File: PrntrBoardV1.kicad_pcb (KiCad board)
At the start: 4 copper layers, 99 x 99 mm, 238 parts, among them J1 EXT 5V, J10 Probe, J11 Extruder Heater, J12 Stepper, J13 Thermistor, J14 Max, J15 Min, J16 Max, J17 Min, J18 Max, J19 Min, J2 Bed Heater, J20 Stepper, J21 Stepper, J22 Stepper, J23 Stepper, J24 Probe, J25 Extruder Heater, J26 Stepper, J27 Thermistor, J28 Thermistor, J29 12-24V, J3 Z Probe, J30 LCD, J31 TC1, J32 TC2, J33 Vin, J34 Vin, J35 5V, J36 5V, J4 E0 Cool, J5 E0 Part, J6 E1 Cool, J7 E1 Part, J8 Always On Fan 1, J9 Always On Fan 2, U1 4078, U11 NUCLEO-64, U2 74HCT02, U3 74LVC125, U4 TMC5130, U5 TMC5130, U6 TMC5130, U7 TMC5130, U8 TMC5130, X1 16MHz

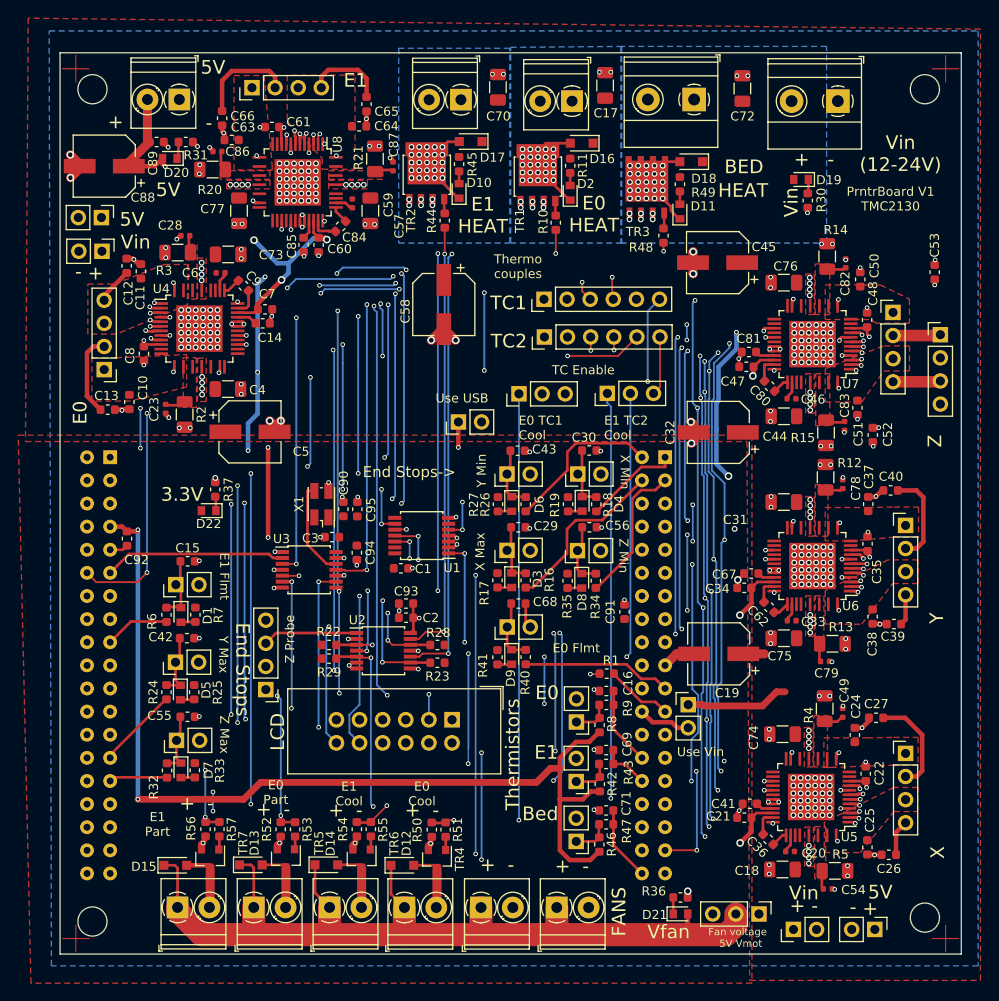
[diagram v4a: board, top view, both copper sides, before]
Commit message: Add thermal releaf on most truehole connectors.
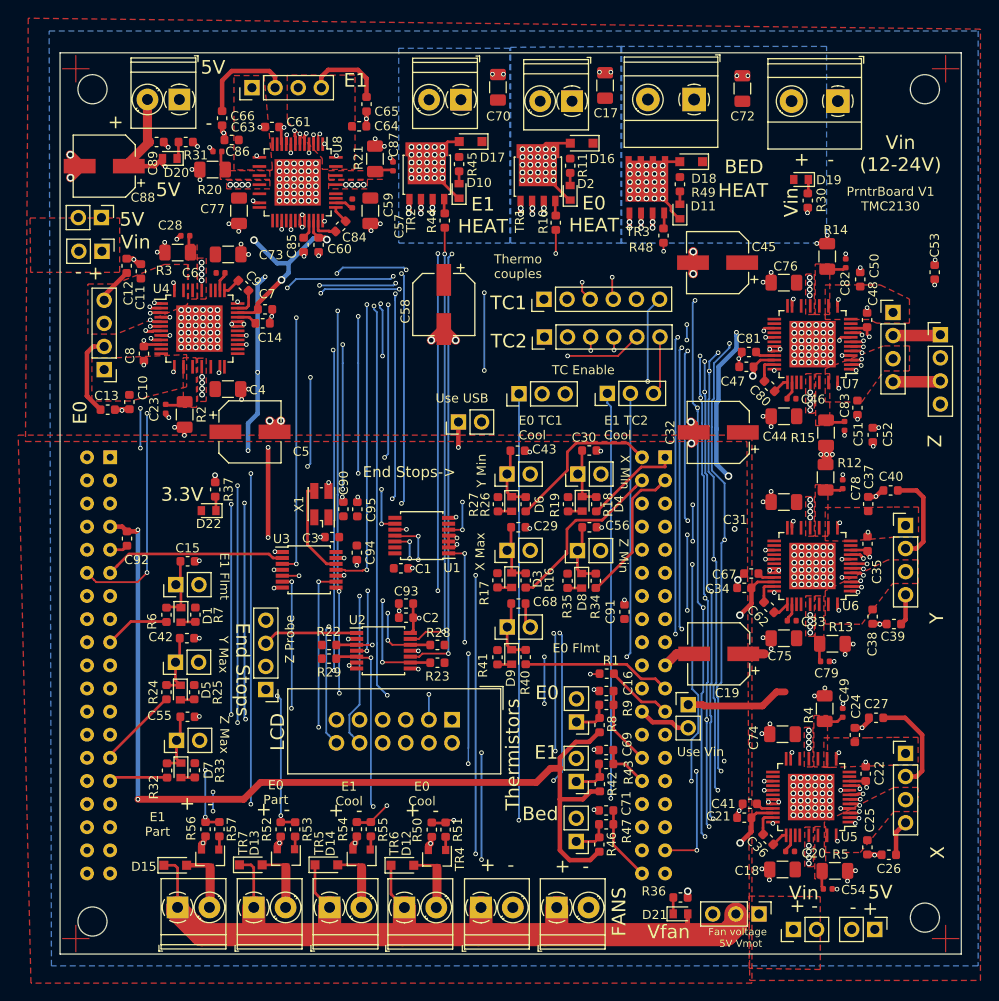
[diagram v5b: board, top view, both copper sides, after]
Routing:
- net GND: track 110.9 -> 170.3 mm, vias 366 -> 365
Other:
- board text added: "(c) iQury.us Aug 2018"
- board text added: "Btn In"
- board text added: "Enc A"
- board text added: "Enc B"
- board text removed: "(c) iQury.us July 2018"

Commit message: Rellocate internal fan connectors, so they are out of the way of the nucleo board. Removed all footprint references from the silk screen.
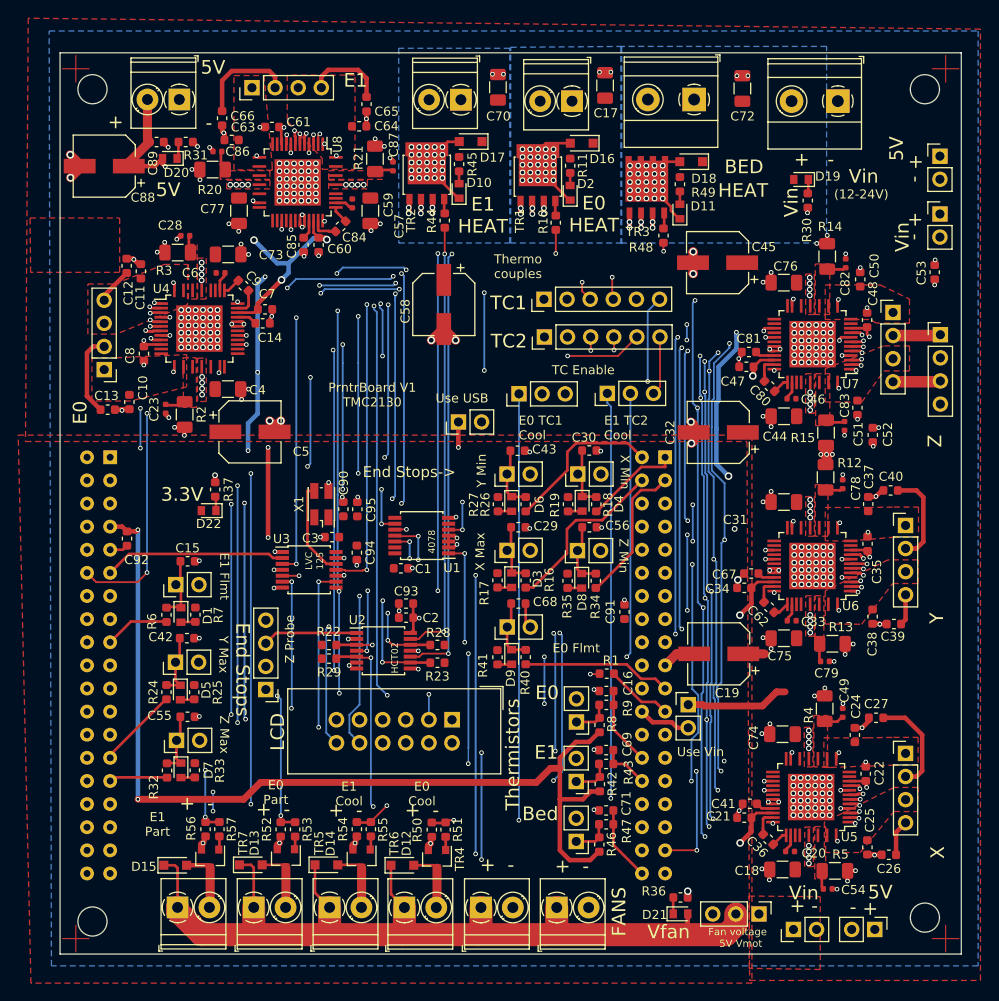
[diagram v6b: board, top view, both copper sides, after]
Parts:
- moved J35 92.4 mm to (116.6, 30.4), turned to 0 degrees
- moved J33 92.1 mm to (116.6, 36.7), turned to 0 degrees
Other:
- board text added: "(12-24V)"
- board text added: "4078"
- board text added: "HCT02"
- board text added: "LVC 125"
- board text removed: "Vin (12-24V)"
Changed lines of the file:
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@@
-(kicad_pcb (version 20171130) (host pcbnew 6.0.0-rc1-unknown-13b9679~65~ubuntu18.04.1)
+(kicad_pcb (version 20171130) (host pcbnew 6.0.0-rc1-unknown-fd3e57d~66~ubuntu18.04.1)
   (general
     (thickness 1.6)
-    (drawings 137)
+    (drawings 142)
     (tracks 2723)
     (zones 0)
@@
   )
   (setup
-    (last_trace_width 0.2032)
+    (last_trace_width 0.1524)
     (user_trace_width 0.1524)
     (user_trace_width 0.2032)
@@
       (psnegative false)
       (psa4output false)
-      (plotreference true)
+      (plotreference false)
       (plotvalue false)
       (plotinvisibletext false)
@@
   )
   (module Connector_PinHeader_2.54mm:PinHeader_1x02_P2.54mm_Vertical (layer F.Cu)
-    (at 24.6 40.8 270)
+    (at 116.6495 36.703)
     (descr "Through hole straight pin header, 1x02, 2.54mm pitch, single row")
     (tags "Through hole pin header THT 1x02 2.54mm single row")
-    (fp_text reference J33 (at -0.1 -0.51 270) (layer F.SilkS) hide
+    (fp_text reference J33 (at -0.1 -0.51) (layer F.SilkS) hide
       (effects (font (size 1 1) (thickness 0.15)))
     )
-    (fp_text value Vin (at 0 4.87 270) (layer F.Fab)
+    (fp_text value Vin (at 0 4.87) (layer F.Fab)
       (effects (font (size 1 1) (thickness 0.15)))
     )
-    (fp_text user %R (at 0 1.27) (layer F.Fab)
+    (fp_text user %R (at 0 1.27 -270) (layer F.Fab)
       (effects (font (size 1 1) (thickness 0.15)))
     )
@@
     (fp_line (start 1.27 -1.27) (end 1.27 3.81) (layer F.Fab) (width 0.1))
     (fp_line (start -0.635 -1.27) (end 1.27 -1.27) (layer F.Fab) (width 0.1))
-    (pad 2 thru_hole oval (at 0 2.54 270) (size 1.7 1.7) (drill 1) (layers *.Cu *.Mask)
+    (pad 2 thru_hole oval (at 0 2.54) (size 1.7 1.7) (drill 1) (layers *.Cu *.Mask)
       (net 8 GND))
-    (pad 1 thru_hole rect (at 0 0 270) (size 1.7 1.7) (drill 1) (layers *.Cu *.Mask)
+    (pad 1 thru_hole rect (at 0 0) (size 1.7 1.7) (drill 1) (layers *.Cu *.Mask)
       (net 1 /V_MOTORS))
     (model ${KISYS3DMOD}/Connector_PinHeader_2.54mm.3dshapes/PinHeader_1x02_P2.54mm_Vertical.wrl
@@
   )
   (module Connector_PinHeader_2.54mm:PinHeader_1x02_P2.54mm_Vertical (layer F.Cu)
-    (at 24.54 37.1 270)
+    (at 116.6495 30.353)
     (descr "Through hole straight pin header, 1x02, 2.54mm pitch, single row")
     (tags "Through hole pin header THT 1x02 2.54mm single row")
-    (fp_text reference J35 (at -0.05 -0.75 270) (layer F.SilkS) hide
+    (fp_text reference J35 (at -0.05 -0.75) (layer F.SilkS) hide
       (effects (font (size 1 1) (thickness 0.15)))
     )
-    (fp_text value 5V (at 0 4.87 270) (layer F.Fab)
+    (fp_text value 5V (at 0 4.87) (layer F.Fab)
       (effects (font (size 1 1) (thickness 0.15)))
     )
-    (fp_text user %R (at 0 1.27) (layer F.Fab)
+    (fp_text user %R (at 0 1.27 -270) (layer F.Fab)
       (effects (font (size 1 1) (thickness 0.15)))
     )
@@
     (fp_line (start 1.27 -1.27) (end 1.27 3.81) (layer F.Fab) (width 0.1))
     (fp_line (start -0.635 -1.27) (end 1.27 -1.27) (layer F.Fab) (width 0.1))
-    (pad 2 thru_hole oval (at 0 2.54 270) (size 1.7 1.7) (drill 1) (layers *.Cu *.Mask)
+    (pad 2 thru_hole oval (at 0 2.54) (size 1.7 1.7) (drill 1) (layers *.Cu *.Mask)
       (net 8 GND))
-    (pad 1 thru_hole rect (at 0 0 270) (size 1.7 1.7) (drill 1) (layers *.Cu *.Mask)
+    (pad 1 thru_hole rect (at 0 0) (size 1.7 1.7) (drill 1) (layers *.Cu *.Mask)
       (net 10 /5V))
     (model ${KISYS3DMOD}/Connector_PinHeader_2.54mm.3dshapes/PinHeader_1x02_P2.54mm_Vertical.wrl
@@
     (tags diode)
     (attr smd)
-    (fp_text reference D19 (at -3.0532 -0.0566 180) (layer F.SilkS)
+    (fp_text reference D19 (at -2.9337 0.3429 180) (layer F.SilkS)
       (effects (font (size 1 1) (thickness 0.15)))
     )
@@
     (tags resistor)
     (attr smd)
-    (fp_text reference R30 (at -0.0548 -1.4916 270) (layer F.SilkS)
+    (fp_text reference R30 (at 3.2512 0.0889 270) (layer F.SilkS)
       (effects (font (size 1 1) (thickness 0.15)))
     )
@@
     (tags capacitor)
     (attr smd)
-    (fp_text reference C53 (at -2.9592 0 270) (layer F.SilkS)
+    (fp_text reference C53 (at 0.08 1.4575 270) (layer F.SilkS)
       (effects (font (size 1 1) (thickness 0.15)))
     )
@@
     (tags resistor)
     (attr smd)
-    (fp_text reference R14 (at 2.919 0.933 -180) (layer F.SilkS)
+    (fp_text reference R14 (at 3.269 0.3175 -180) (layer F.SilkS)
       (effects (font (size 1 1) (thickness 0.15)))
     )
@@
     )
   )
+  (gr_text "LVC\n125" (at 47.9425 74.803 90) (layer F.SilkS)
+    (effects (font (size 0.75 0.75) (thickness 0.15)))
+  )
+  (gr_text 4078 (at 60.833 72.7075 90) (layer F.SilkS)
+    (effects (font (size 0.75 0.75) (thickness 0.15)))
+  )
+  (gr_text HCT02 (at 56.769 85.471 90) (layer F.SilkS)
+    (effects (font (size 0.75 0.75) (thickness 0.15)))
+  )
+  (gr_text "+ -" (at 114.046 31.6865 270) (layer F.SilkS)
+    (effects (font (size 1.5 1.5) (thickness 0.3)))
+  )
+  (gr_text "(12-24V)" (at 108.0135 34.544) (layer F.SilkS)
+    (effects (font (size 1 1) (thickness 0.25)))
+  )
   (gr_text GND (at 50.3555 89.662 90) (layer B.SilkS)
     (effects (font (size 1 1) (thickness 0.15)) (justify mirror))
@@
   (gr_line (start 56 27) (end 56 55) (layer B.SilkS) (width 0.15))
   (gr_line (start 28 27) (end 56 27) (layer B.SilkS) (width 0.15))
-  (gr_text "+ -" (at 23.1 34.8) (layer B.SilkS)
+  (gr_text "+ -" (at 113.8555 31.6865 90) (layer B.SilkS)
     (effects (font (size 1.5 1.5) (thickness 0.3)) (justify mirror))
   )
-  (gr_text Vin (at 26.035 42.799) (layer B.SilkS)
+  (gr_text Vin (at 112.014 38.1635 90) (layer B.SilkS)
     (effects (font (size 1.5 1.5) (thickness 0.3)) (justify mirror))
   )
-  (gr_text "+ -" (at 23.1 38.9) (layer B.SilkS)
+  (gr_text "+ -" (at 113.792 38.0365 90) (layer B.SilkS)
     (effects (font (size 1.5 1.5) (thickness 0.3)) (justify mirror))
   )
-  (gr_text 5V (at 26.289 33.4645) (layer B.SilkS)
+  (gr_text 5V (at 112.141 31.8135 90) (layer B.SilkS)
     (effects (font (size 1.5 1.5) (thickness 0.3)) (justify mirror))
   )
@@
     (effects (font (size 1 1) (thickness 0.15)) (justify mirror))
   )
-  (gr_text Vin (at 28.3 39.8) (layer F.SilkS)
+  (gr_text Vin (at 112.522 39.243 90) (layer F.SilkS)
     (effects (font (size 1.5 1.5) (thickness 0.3)))
   )
-  (gr_text "+ -" (at 23.2 43.3 180) (layer F.SilkS)
+  (gr_text "+ -" (at 113.9825 38.0365 270) (layer F.SilkS)
     (effects (font (size 1.5 1.5) (thickness 0.3)))
   )
-  (gr_text 5V (at 27.9 37.3) (layer F.SilkS)
+  (gr_text 5V (at 111.887 29.5275 90) (layer F.SilkS)
     (effects (font (size 1.5 1.5) (thickness 0.3)))
   )
@@
     (effects (font (size 1 1) (thickness 0.2)))
   )
-  (gr_text "Vin\n(12-24V)" (at 112.3188 30.0736) (layer F.SilkS)
+  (gr_text Vin (at 108.2675 32.5755) (layer F.SilkS)
     (effects (font (size 1.5 1.5) (thickness 0.3)))
   )
@@
     (effects (font (size 1 1) (thickness 0.15)) (justify mirror))
   )
-  (gr_text "rev 3" (at 116.3 32.1 90) (layer B.SilkS)
+  (gr_text "rev 3" (at 103.3145 32.4485) (layer B.SilkS)
     (effects (font (size 1.5 1.5) (thickness 0.3)) (justify mirror))
   )
-  (gr_text "(c) iQury.us\nAug 2018" (at 113 32.5 90) (layer B.SilkS)
+  (gr_text "(c) iQury.us\nAug 2018" (at 103.124 35.4965) (layer B.SilkS)
     (effects (font (size 1 1) (thickness 0.15)) (justify mirror))
   )
-  (gr_text "PrntrBoard V1\nTMC2130" (at 111.2266 35.052) (layer F.SilkS)
+  (gr_text "PrntrBoard V1\nTMC2130" (at 54.2925 56.5785) (layer F.SilkS)
     (effects (font (size 1 1) (thickness 0.15)))
   )
@@
     (effects (font (size 1.5 1.5) (thickness 0.3)) (justify mirror))
   )
-  (gr_text "Z Axis" (at 114.2 43.9 90) (layer B.SilkS)
+  (gr_text "Z Axis" (at 114.7445 44.5135 90) (layer B.SilkS)
     (effects (font (size 1.5 1.5) (thickness 0.3)) (justify mirror))
   )

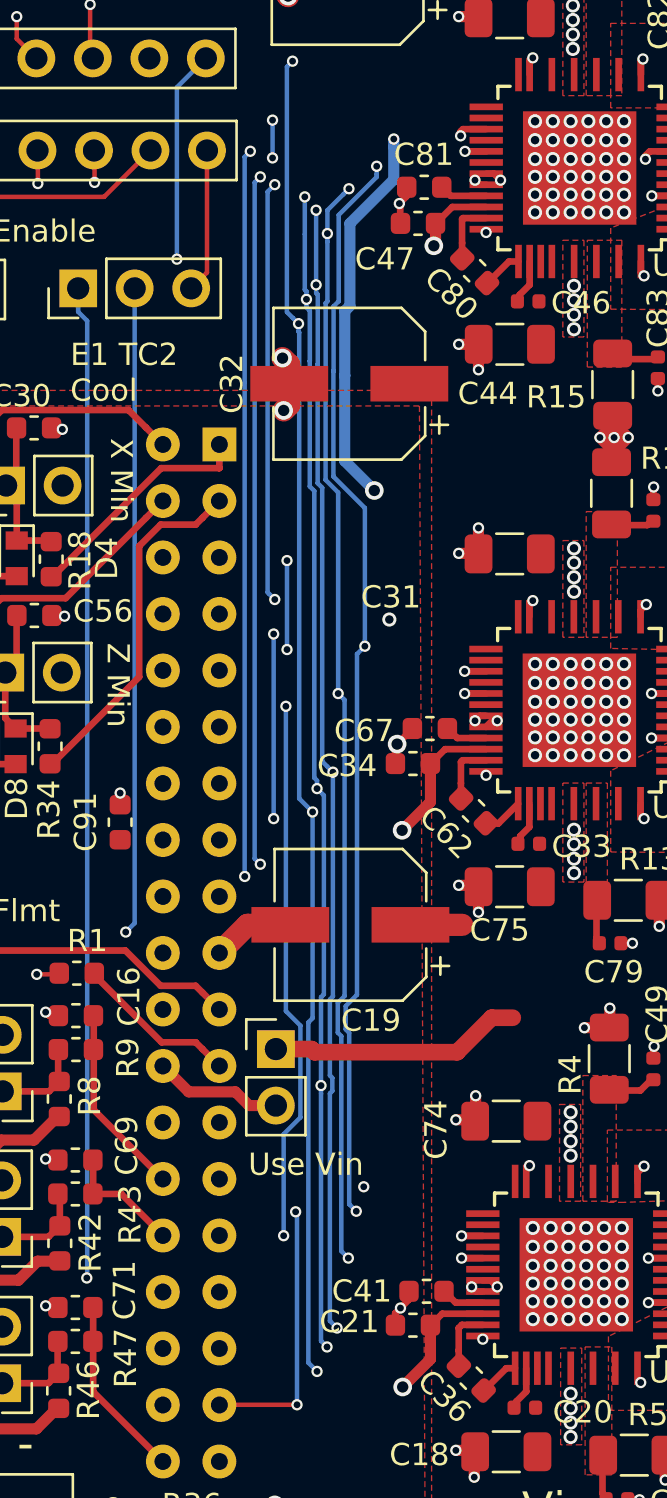
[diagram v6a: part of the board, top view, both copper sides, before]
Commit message: Update some signal traces to wiggle less.
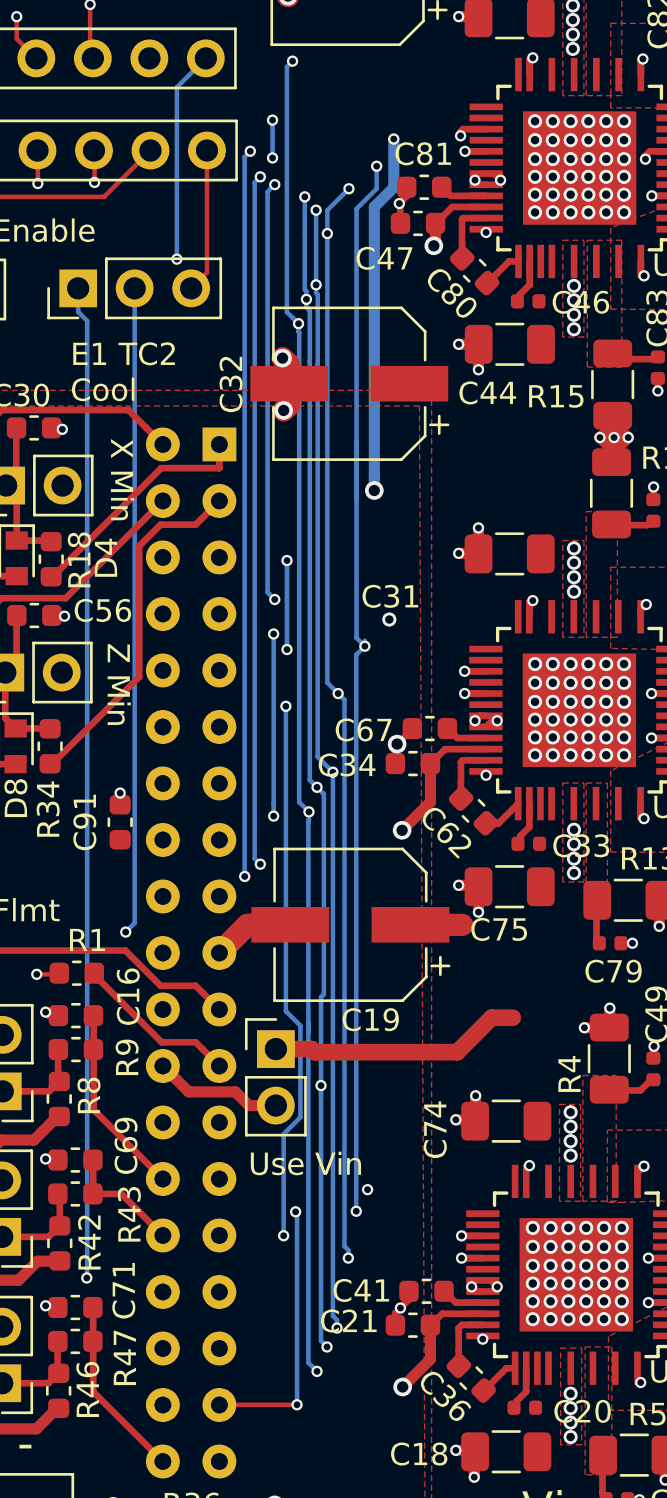
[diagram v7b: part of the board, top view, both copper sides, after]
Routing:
- net /MISO: track 229.5 -> 231.0 mm
- net /3.3V: track 132.5 -> 131.5 mm
